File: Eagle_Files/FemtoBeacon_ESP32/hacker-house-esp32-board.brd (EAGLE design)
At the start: 42.4 x 82.3 mm, 56 parts, among them IC1 FT232RQ

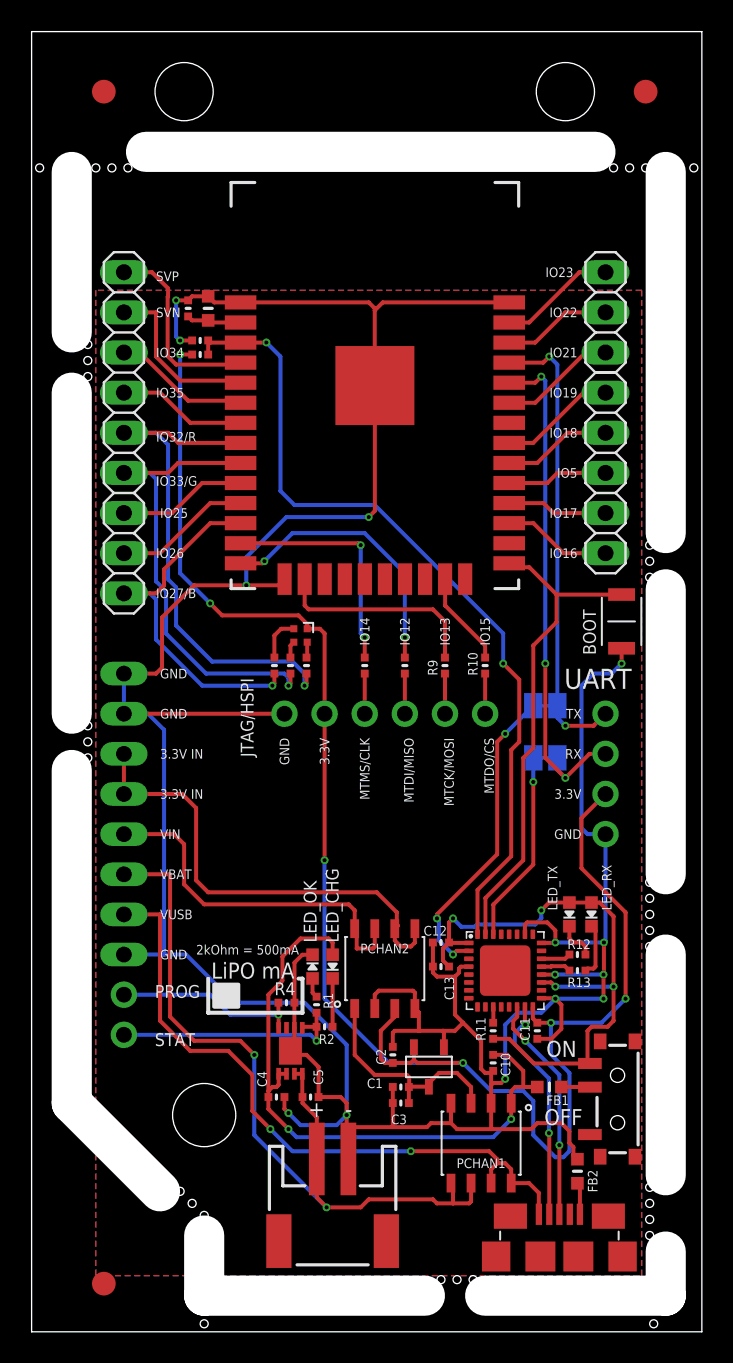
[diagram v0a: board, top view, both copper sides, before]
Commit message: Revised BoM for the Hacker.House board, fixed missing 3V3 trace with 2.0.1 design of Hacker.House board (version bump to 2.0.2)
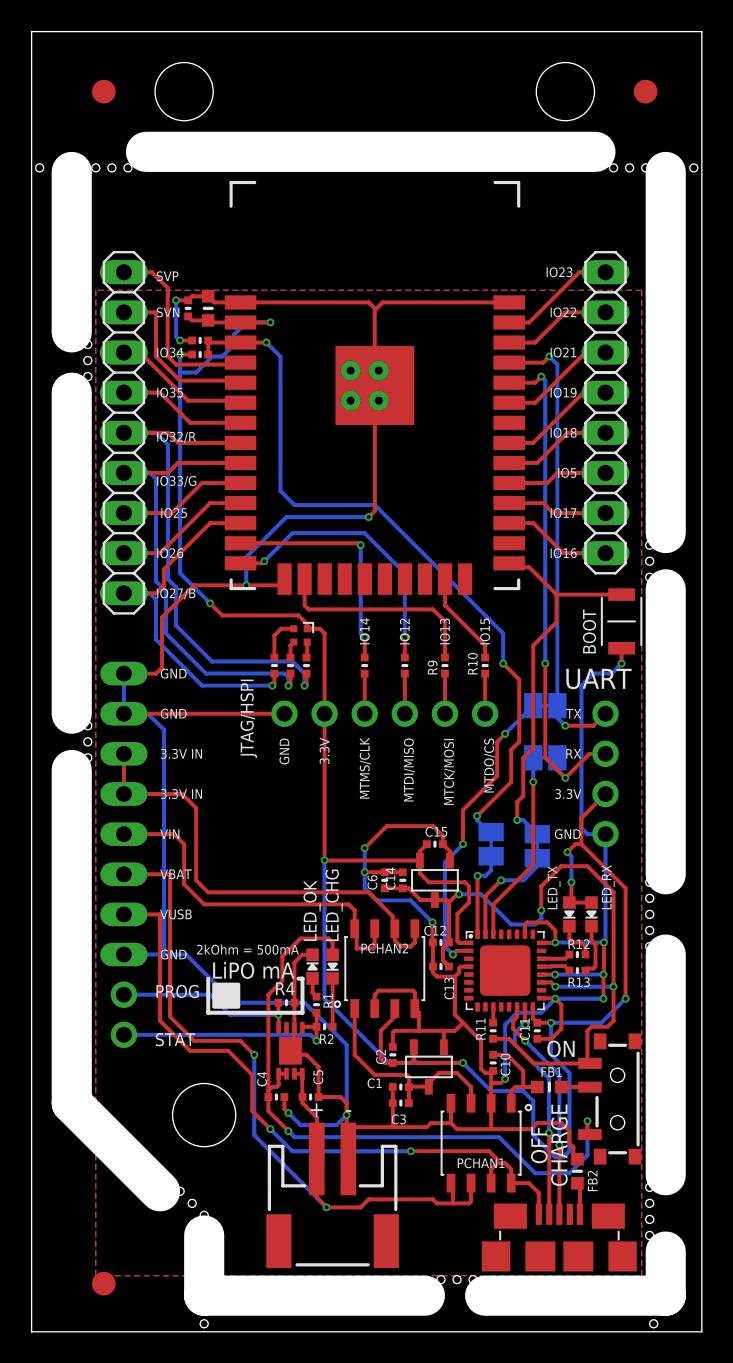
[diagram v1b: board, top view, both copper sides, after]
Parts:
- added C14, C15: 2.2uF, microbuilder:_0402MP
- added C6: 0.47uF, microbuilder:_0402MP
- added DTR, RTS: DNP, microbuilder:SOLDERJUMPER_CLOSEDWIRE
- added LDO2: 3.3V, MCP1700T-3302E_TT:MCP1700T-3302E/TT
- MOD1: device esp32-wroom-32:ESP32-WROOM-32-MODULE -> esp32-wroom-32-managed:ESP32-WROOM-32-MODULE
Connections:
- removed net GND: BOOT.2, C1.2, C10.1, C11.1, C12.1, C13.1, C2.2, C3.2, C4.2, C5.2, C7.1, C8.1, C9.1, CN_LIPO.1, FB2.2, IC1.17, IC1.20, IC1.24, IC1.26, IC1.4, JTAG/HSPI.1, LDO1.GND, LED_OK.C, LIPO1.6, LIPO1.9, MOD1.1, MOD1.15, MOD1.38, MOD1.GND, PCHAN1.2, PCHAN1.4, PCHAN2.2, PCHAN2.4, POWER.1, POWER.7, POWER.8, R4.2, UART.1
- removed net VCC: C7.2, C8.2, MOD1.2
- new net GND_UNMASKED: BOOT.2, C1.2, C10.1, C11.1, C12.1, C13.1, C14.2, C15.2, C2.2, C3.2, C4.2, C5.2, C6.2, C7.1, C8.1, C9.1, CN_LIPO.1, FB2.2, IC1.17, IC1.20, IC1.24, IC1.26, IC1.4, JTAG/HSPI.1, LDO1.GND, LDO2.GND, LED_OK.C, LIPO1.6, LIPO1.9, MOD1.1, MOD1.15, MOD1.38, MOD1.GND, PCHAN1.2, PCHAN1.4, PCHAN2.2, PCHAN2.4, POWER.1, POWER.7, POWER.8, R4.2, UART.1
- new net VUSB_CHG_LIPO: C4.1, LED_CHG.A, LIPO1.1, LIPO1.2, SWPOWER.A
- net 3.3V: now also C15.1, C7.2, C8.2, IC1.1, LDO2.VOUT, LED_RX.A, LED_TX.A, MOD1.2
- net BOOT/DTR: now also DTR.1, DTR.2
- net EN/RTS: now also RTS.1, RTS.2
- net VPWR: now also C14.1, C6.1, LDO2.VIN; no longer IC1.1, LED_RX.A, LED_TX.A
- net VUSB: no longer C4.1, LED_CHG.A, LIPO1.1, LIPO1.2
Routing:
- net GND_UNMASKED: track 0.00 -> 265.0 mm, vias 0 -> 21
- net GND: track 238.5 -> 0.00 mm, vias 14 -> 0
- net VUSB_CHG_LIPO: track 0.00 -> 42.1 mm, vias 0 -> 2
- net 3.3V: track 110.2 -> 144.9 mm, vias 6 -> 9
- net VUSB: track 40.0 -> 5.87 mm, vias 2 -> 0
- net VPWR: track 38.5 -> 47.2 mm
- net VCC: track 3.48 -> 0.00 mm
- net BOOT/DTR: track 31.3 -> 33.4 mm, vias 0 -> 2
- net EN/RTS: track 52.8 -> 53.9 mm, vias 2 -> 4
- added copper zone on layer 1, net GND_UNMASKED
- added copper zone on layer 16, net GND_UNMASKED
- removed copper zone on layer 1, net GND
- removed copper zone on layer 16, net GND
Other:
- board text added: "2.0.2"
- board text added: "CHARGE"
- board text removed: "2.0.0"
